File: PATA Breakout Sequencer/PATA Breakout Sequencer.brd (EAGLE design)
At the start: 100 x 70 mm, 57 parts, among them IC1 74HC165N, IC2 74HC165N, IC3 74HC165N, IC4 74HC165N, IC5 74HC165N

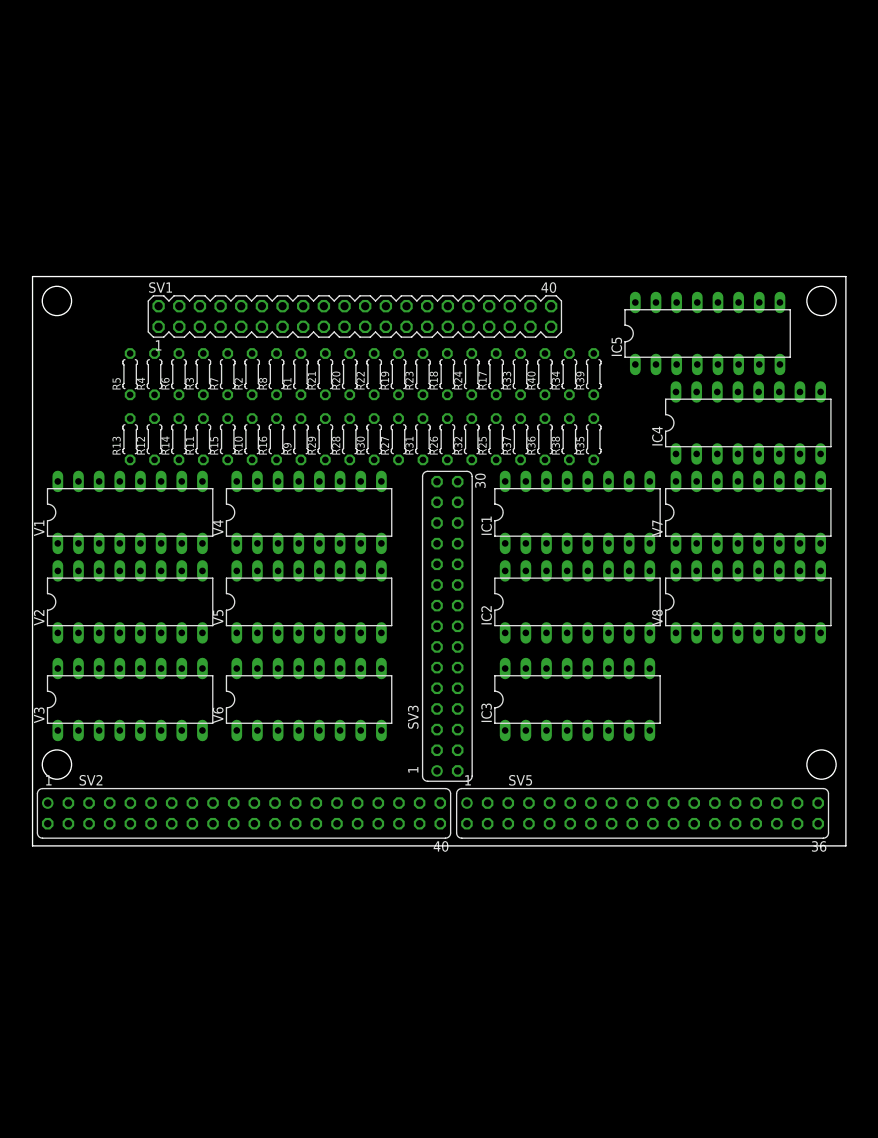
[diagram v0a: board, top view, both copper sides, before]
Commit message: split board into 2
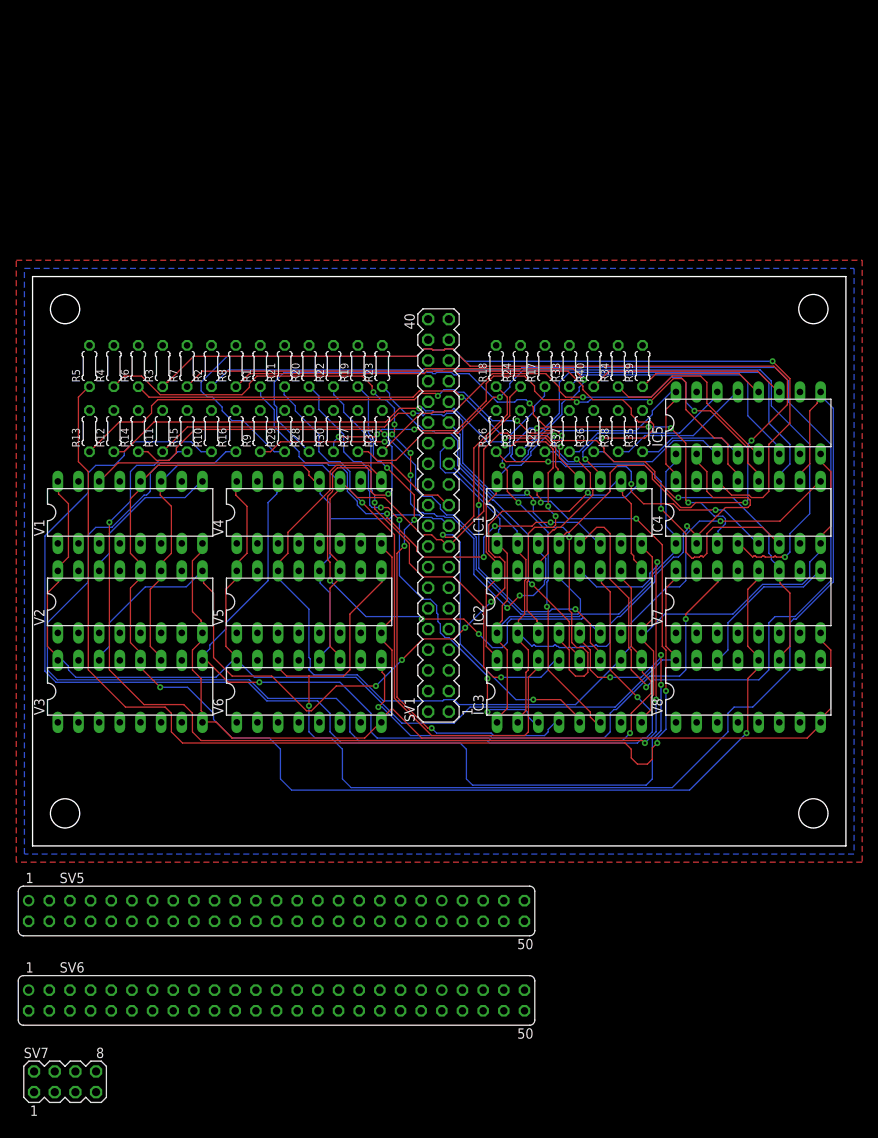
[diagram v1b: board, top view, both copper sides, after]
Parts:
- removed SV2: (no value), con-lsta:FE20-2
- removed SV3: (no value), con-lsta:FE15-2
- added SV6: (no value), con-lsta:FE25-2
- added SV7: (no value), con-lstb:MA04-2
- SV5: device con-lsta:FE18-2 -> con-lsta:FE25-2
- moved SV5 46.6 mm to (30.0, -8.00)
- moved SV1 26.5 mm to (49.9, 40.6), turned to 90 degrees
- moved IC5 12.1 mm to (88.0, 52.0)
- moved IC4 11.0 mm to (88.0, 41.0)
- moved V7 11.0 mm to (88.0, 30.0)
- moved V8 11.0 mm to (88.0, 19.0)
- moved R17 6.08 mm to (63.0, 59.0)
- moved R18 6.08 mm to (57.0, 59.0)
- moved R24 6.08 mm to (60.0, 59.0)
- moved R25 6.08 mm to (63.0, 51.0)
- moved R26 6.08 mm to (57.0, 51.0)
- moved R32 6.08 mm to (60.0, 51.0)
- moved R33 6.08 mm to (66.0, 59.0)
- moved R34 6.08 mm to (72.0, 59.0)
- moved R35 6.08 mm to (75.0, 51.0)
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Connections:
- removed net N$10: SV3.16
- removed net N$11: SV3.14
- removed net N$12: SV3.12
- removed net N$13: SV3.10
- removed net N$14: SV3.8
- removed net N$15: SV3.6
- removed net N$16: SV3.4
- removed net N$17: SV3.2
- removed net N$21: SV3.29
- removed net N$22: SV3.27
- removed net N$23: SV3.25
- removed net N$24: SV3.23
- removed net N$25: SV3.21
- removed net N$26: SV3.19
- removed net N$27: SV3.17
- removed net N$4: SV3.28
- removed net N$5: SV3.26
- removed net N$6: SV3.24
- removed net N$7: SV3.22
- removed net N$8: SV3.20
- removed net N$9: SV3.18
- net A0: now also SV6.1; no longer SV3.1, SV3.30
- net A1: now also SV6.17
- net A10: now also SV5.34
- net A11: now also SV5.50
- net A2: now also SV6.2
- net A3: now also SV5.1, SV6.18
- net A4: now also SV5.2
- net A5: now also SV5.17
- net A6: now also SV5.18
- net A7: now also SV6.33
- net A8: now also SV6.34
- net A9: now also SV5.33
- net B0: now also SV6.3; no longer SV3.3
- net B1: now also SV6.19
- net B10: now also SV5.36
- net B11: now also SV5.49
- net B2: now also SV6.4
- net B3: now also SV5.3, SV6.20
- net B4: now also SV5.4
- net B5: now also SV5.19
- net B6: now also SV5.20
- net B7: now also SV6.35
- net B8: now also SV6.36
- net B9: now also SV5.35
- net C0: now also SV6.5; no longer SV3.5
- net C1: now also SV6.21
- net C10: now also SV5.38
- net C11: now also SV6.50
- net C2: now also SV6.6
- net C3: now also SV5.5, SV6.22
- net C4: now also SV5.6
- net C5: now also SV5.21
- net C6: now also SV5.22
- net C7: now also SV6.37
- net C8: now also SV6.38
- net C9: now also SV5.37
- net D0: now also SV6.7; no longer SV3.7
- net D1: now also SV6.23
- net D10: now also SV5.40
- net D11: now also SV6.49
- net D2: now also SV6.8
- net D3: now also SV5.7, SV6.24
- net D4: now also SV5.8
- net D5: now also SV5.23
- net D6: now also SV5.24
- net D7: now also SV6.39
- net D8: now also SV6.40
- net D9: now also SV5.39
- net E0: now also SV6.9; no longer SV3.9
- net E1: now also SV6.25
- net E10: now also SV5.42
- net E11: now also SV7.8
- net E2: now also SV6.10
- net E3: now also SV5.9, SV6.26
- net E4: now also SV5.10
- net E5: now also SV5.25
- net E6: now also SV5.26
- net E7: now also SV6.41
- net E8: now also SV6.42
- net E9: now also SV5.41
- net F0: now also SV6.11; no longer SV3.11
- net F1: now also SV6.27
- net F10: now also SV5.44
- net F11: now also SV7.7
- net F2: now also SV6.12
- net F3: now also SV5.11, SV6.28
- net F4: now also SV5.12
- net F5: now also SV5.27
- net F6: now also SV5.28
- net F7: now also SV6.43
- net F8: now also SV6.44
- net F9: now also SV5.43
- net G0: now also SV6.13; no longer SV3.13
- net G1: now also SV6.29
- net G10: now also SV5.46
- net G11: now also SV7.6
- net G2: now also SV6.14
- net G3: now also SV5.13, SV6.30
- net G4: now also SV5.14
- net G5: now also SV5.29
- net G6: now also SV5.30
- net G7: now also SV6.45
- net G8: now also SV6.46
- net G9: now also SV5.45
- net H0: now also SV6.15; no longer SV3.15
- net H1: now also SV6.31
- net H10: now also SV5.48
- net H11: now also SV7.5
- net H2: now also SV6.16
- net H3: now also SV5.15, SV6.32
- net H4: now also SV5.16
- net H5: now also SV5.31
- net H6: now also SV5.32
- net H7: now also SV6.47
- net H8: now also SV6.48
- net H9: now also SV5.47
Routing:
- net LATCH_OUT: track 0.00 -> 196.4 mm, vias 0 -> 2
- net SHIFT_OUT: track 0.00 -> 161.6 mm, vias 0 -> 1
- net D0: track 0.00 -> 159.6 mm, vias 0 -> 4
- net G1: track 0.00 -> 159.5 mm, vias 0 -> 3
- net G0: track 0.00 -> 156.7 mm, vias 0 -> 1
- net OUT4: track 0.00 -> 151.9 mm, vias 0 -> 1
- net +UB: track 0.00 -> 145.1 mm
- net A1: track 0.00 -> 144.9 mm, vias 0 -> 1
- net B1: track 0.00 -> 139.5 mm, vias 0 -> 4
- net -UB: track 0.00 -> 139.2 mm
- net F0: track 0.00 -> 129.0 mm, vias 0 -> 2
- net OUT3: track 0.00 -> 117.9 mm, vias 0 -> 1
- net OUT1: track 0.00 -> 115.3 mm, vias 0 -> 5
- net D3: track 0.00 -> 112.9 mm, vias 0 -> 1
- net OUT2: track 0.00 -> 106.8 mm, vias 0 -> 2
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- added copper zone on layer 1, net +5V
- added copper zone on layer 16, net DGND

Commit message: Finished top board - ran DRC
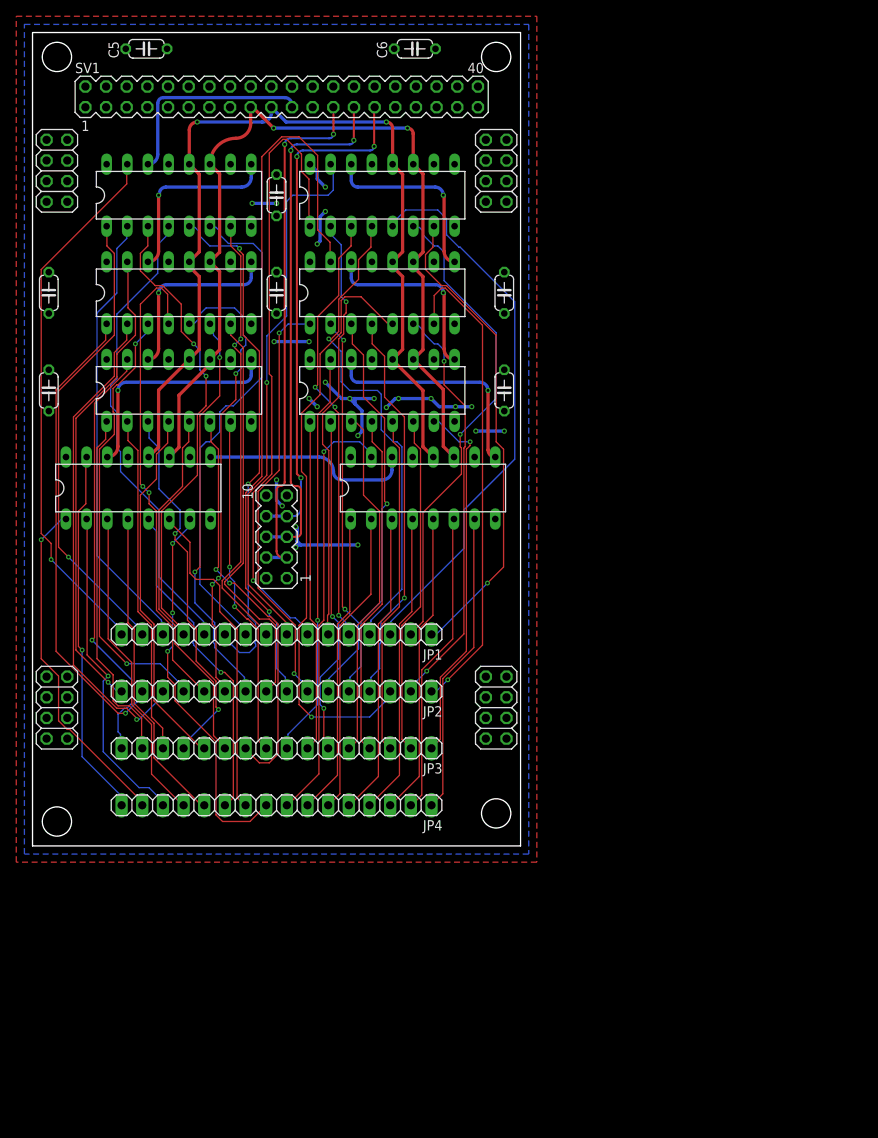
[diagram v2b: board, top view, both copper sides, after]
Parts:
- removed IC1, IC2, IC3, IC4, IC5: 74HC165N, 74xx-eu:DIL16
- removed R1, R10, R11, R12, R13, R14, R15, R16, R17, R18, R19, R2, R20, R21, R22, R23, R24, R25, R26, R27, R28, R29, R3, R30, R31, R32, R33, R34, R35, R36, R37, R38, R39, R4, R40, R5, R6, R7, R8, R9: (no value), rcl:0204/5
- removed SV5, SV6: (no value), con-lsta:FE25-2
- removed SV7: (no value), con-lstb:MA04-2
- added C1, C2, C3, C4, C5, C6, C7, C8: 4.7uF, rcl:C050-024X044
- added JP1, JP2, JP3, JP4: (no value), pinhead:1X16
- added JP6, JP7, JP8, JP9: (no value), pinhead:2X04
- added SV3: (no value), con-lstb:MA05-2
- moved V8 75.8 mm to (43.0, 80.0)
- moved V7 58.9 mm to (43.0, 68.0)
- moved SV1 55.0 mm to (30.6, 92.1), turned to 0 degrees
- moved V1 39.5 mm to (18.0, 80.0)
- moved V2 38.5 mm to (18.0, 68.0)
- moved V6 38.1 mm to (43.0, 56.0)
- moved V3 37.5 mm to (18.0, 56.0)
- moved V4 21.2 mm to (13.0, 44.0)
- moved V5 19.8 mm to (48.0, 44.0)
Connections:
- removed net +5V: R1.2, R10.2, R11.2, R12.2, R13.2, R14.2, R15.2, R16.2, R17.2, R18.2, R19.2, R2.2, R20.2, R21.2, R22.2, R23.2, R24.2, R25.2, R26.2, R27.2, R28.2, R29.2, R3.2, R30.2, R31.2, R32.2, R33.2, R34.2, R35.2, R36.2, R37.2, R38.2, R39.2, R4.2, R40.2, R5.2, R6.2, R7.2, R8.2, R9.2, SV1.2, SV1.4, SV1.6
- removed net A0: IC1.11, R8.1, SV6.1
- removed net A1: IC2.11, R16.1, SV6.17
- removed net A2: IC3.11, R24.1, SV6.2
- removed net A3: IC4.11, R32.1, SV5.1, SV6.18
- removed net A4: IC5.11, R40.1, SV5.2
- removed net B0: IC1.12, R7.1, SV6.3
- removed net B1: IC2.12, R15.1, SV6.19
- removed net B2: IC3.12, R23.1, SV6.4
- removed net B3: IC4.12, R31.1, SV5.3, SV6.20
- removed net B4: IC5.12, R39.1, SV5.4
- removed net C0: IC1.13, R6.1, SV6.5
- removed net C1: IC2.13, R14.1, SV6.21
- removed net C2: IC3.13, R22.1, SV6.6
- removed net C3: IC4.13, R30.1, SV5.5, SV6.22
- removed net C4: IC5.13, R38.1, SV5.6
- removed net D0: IC1.14, R5.1, SV6.7
- removed net D1: IC2.14, R13.1, SV6.23
- removed net D2: IC3.14, R21.1, SV6.8
- removed net D3: IC4.14, R29.1, SV5.7, SV6.24
- removed net D4: IC5.14, R37.1, SV5.8
- removed net DGND: IC1.15, IC2.15, IC3.15, IC4.15, IC5.10, IC5.15, SV1.1, SV1.10, SV1.11, SV1.12, SV1.14, SV1.15, SV1.16, SV1.18, SV1.20, SV1.22, SV1.23, SV1.24, SV1.26, SV1.28, SV1.3, SV1.30, SV1.31, SV1.32, SV1.33, SV1.34, SV1.5, SV1.7, SV1.8, V1.13, V2.13, V3.13, V4.13, V5.13, V6.13, V7.13, V8.13
- removed net E0: IC1.3, R4.1, SV6.9
- removed net E1: IC2.3, R12.1, SV6.25
- removed net E2: IC3.3, R20.1, SV6.10
- removed net E3: IC4.3, R28.1, SV5.9, SV6.26
- removed net E4: IC5.3, R36.1, SV5.10
- removed net F0: IC1.4, R3.1, SV6.11
- removed net F1: IC2.4, R11.1, SV6.27
- removed net F2: IC3.4, R19.1, SV6.12
- removed net F3: IC4.4, R27.1, SV5.11, SV6.28
- removed net F4: IC5.4, R35.1, SV5.12
- removed net G0: IC1.5, R2.1, SV6.13
- removed net G1: IC2.5, R10.1, SV6.29
- removed net G2: IC3.5, R18.1, SV6.14
- removed net G3: IC4.5, R26.1, SV5.13, SV6.30
- removed net G4: IC5.5, R34.1, SV5.14
- removed net GND: IC1.8, IC2.8, IC3.8, IC4.8, IC5.8
- removed net H0: IC1.6, R1.1, SV6.15
- removed net H1: IC2.6, R9.1, SV6.31
- removed net H2: IC3.6, R17.1, SV6.16
- removed net H3: IC4.6, R25.1, SV5.15, SV6.32
- removed net H4: IC5.6, R33.1, SV5.16
- removed net VCC: IC1.16, IC2.16, IC3.16, IC4.16, IC5.16
- net +UB: now also C1.1, C2.1, C3.1, C4.1, C5.1, C6.1, C7.1, C8.1, JP6.1, JP6.3, JP6.5, JP6.7, JP7.1, JP7.3, JP7.5, JP7.7, JP8.1, JP8.3, JP8.5, JP8.7, JP9.1, JP9.3, JP9.5, JP9.7, SV1.2, SV1.4, SV1.6, SV3.2, SV3.9
- net -UB: now also C1.2, C2.2, C3.2, C4.2, C5.2, C6.2, C7.2, C8.2, JP6.2, JP6.4, JP6.6, JP6.8, JP7.2, JP7.4, JP7.6, JP7.8, JP8.2, JP8.4, JP8.6, JP8.8, JP9.2, JP9.4, JP9.6, JP9.8, SV1.1, SV1.10, SV1.11, SV1.12, SV1.14, SV1.15, SV1.16, SV1.18, SV1.20, SV1.22, SV1.23, SV1.24, SV1.26, SV1.28, SV1.3, SV1.30, SV1.31, SV1.32, SV1.33, SV1.34, SV1.5, SV1.7, SV1.8, SV3.1, SV3.10, V1.13, V2.13, V3.13, V4.13, V5.13, V6.13, V7.13, V8.13
- net A10: now also JP3.8; no longer SV5.34
- net A11: now also JP2.8; no longer SV5.50
- net A12: now also JP1.8
- net A5: now also JP1.16; no longer SV5.17
- net A6: now also JP2.16; no longer SV5.18
- net A7: now also JP3.16; no longer SV6.33
- net A8: now also JP4.16; no longer SV6.34
- net A9: now also JP4.8; no longer SV5.33
- net B10: now also JP3.7; no longer SV5.36
- net B11: now also JP2.7; no longer SV5.49
- net B12: now also JP1.7
- net B5: now also JP1.15; no longer SV5.19
- net B6: now also JP2.15; no longer SV5.20
- net B7: now also JP3.15; no longer SV6.35
- net B8: now also JP4.15; no longer SV6.36
- net B9: now also JP4.7; no longer SV5.35
- net C10: now also JP3.6; no longer SV5.38
- net C11: now also JP2.6; no longer SV6.50
- net C12: now also JP1.6
- net C5: now also JP1.14; no longer SV5.21
- net C6: now also JP2.14; no longer SV5.22
- net C7: now also JP3.14; no longer SV6.37
- net C8: now also JP4.14; no longer SV6.38
- net C9: now also JP4.6; no longer SV5.37
- net D10: now also JP3.5; no longer SV5.40
- net D11: now also JP2.5; no longer SV6.49
- net D12: now also JP1.5
- net D5: now also JP1.13; no longer SV5.23
- net D6: now also JP2.13; no longer SV5.24
- net D7: now also JP3.13; no longer SV6.39
- net D8: now also JP4.13; no longer SV6.40
- net D9: now also JP4.5; no longer SV5.39
- net E10: now also JP3.4; no longer SV5.42
- net E11: now also JP2.4; no longer SV7.8
- net E12: now also JP1.4
- net E5: now also JP1.12; no longer SV5.25
- net E6: now also JP2.12; no longer SV5.26
- net E7: now also JP3.12; no longer SV6.41
- net E8: now also JP4.12; no longer SV6.42
- net E9: now also JP4.4; no longer SV5.41
- net F10: now also JP3.3; no longer SV5.44
- net F11: now also JP2.3; no longer SV7.7
- net F12: now also JP1.3
- net F5: now also JP1.11; no longer SV5.27
- net F6: now also JP2.11; no longer SV5.28
- net F7: now also JP3.11; no longer SV6.43
- net F8: now also JP4.11; no longer SV6.44
- net F9: now also JP4.3; no longer SV5.43
- net G10: now also JP3.2; no longer SV5.46
- net G11: now also JP2.2; no longer SV7.6
- net G12: now also JP1.2
- net G5: now also JP1.10; no longer SV5.29
- net G6: now also JP2.10; no longer SV5.30
- net G7: now also JP3.10; no longer SV6.45
- net G8: now also JP4.10; no longer SV6.46
- net G9: now also JP4.2; no longer SV5.45
- net H10: now also JP3.1; no longer SV5.48
- net H11: now also JP2.1; no longer SV7.5
- net H12: now also JP1.1
- net H5: now also JP1.9; no longer SV5.31
- net H6: now also JP2.9; no longer SV5.32
- net H7: now also JP3.9; no longer SV6.47
- net H8: now also JP4.9; no longer SV6.48
- net H9: now also JP4.1; no longer SV5.47
- net LATCH_IN: now also SV3.5, SV3.6; no longer IC1.1, IC2.1, IC3.1, IC4.1, IC5.1
- net OUT1: no longer IC1.10, IC2.9
- net OUT2: no longer IC2.10, IC3.9
- net OUT3: no longer IC3.10, IC4.9
- net OUT4: no longer IC4.10, IC5.9
- net SERIAL_IN: now also SV3.7, SV3.8; no longer IC1.9
- net SHIFT_IN: now also SV3.3, SV3.4; no longer IC1.2, IC2.2, IC3.2, IC4.2, IC5.2
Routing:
- net D0: track 159.6 -> 0.00 mm, vias 4 -> 0
- net G1: track 159.5 -> 0.00 mm, vias 3 -> 0
- net G0: track 156.7 -> 0.00 mm, vias 1 -> 0
- net A1: track 144.9 -> 0.00 mm, vias 1 -> 0
- net B1: track 139.5 -> 0.00 mm, vias 4 -> 0
- net -UB: track 139.2 -> 0.00 mm
- net F0: track 129.0 -> 0.00 mm, vias 2 -> 0
- net OUT4: track 151.9 -> 28.1 mm
- net D3: track 112.9 -> 0.00 mm, vias 1 -> 0
- net OUT1: track 115.3 -> 22.8 mm, vias 5 -> 1
- net OUT3: track 117.9 -> 25.6 mm, vias 1 -> 0
- net A11: track 0.00 -> 91.3 mm, vias 0 -> 1
- net F1: track 89.2 -> 0.00 mm, vias 4 -> 0
- net F3: track 88.6 -> 0.00 mm, vias 2 -> 0
- net H1: track 87.1 -> 0.00 mm, vias 5 -> 0
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- added copper zone on layer 1, net +UB
- added copper zone on layer 16, net -UB
- removed copper zone on layer 1, net +5V
- removed copper zone on layer 16, net DGND
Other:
- board size 100 x 70 mm -> 60 x 100 mm

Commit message: cleanup
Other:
- board text added: "1"
- board text added: "A"
- board text added: "H"
- board text added: "Koltin Kosik-Harvey March 7 / 2019"
- board text added: "PATA Sequencer Breakout TOP"
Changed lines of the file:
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@@
 <hole x="57" y="4" drill="3.6"/>
 <hole x="57" y="97" drill="3.6"/>
+<wire x1="30" y1="30" x2="30" y2="24" width="0.1524" layer="21"/>
+<wire x1="30" y1="21" x2="30" y2="17" width="0.1524" layer="21"/>
+<wire x1="30" y1="14" x2="30" y2="10" width="0.1524" layer="21"/>
+<wire x1="30" y1="7" x2="30" y2="3" width="0.1524" layer="21"/>
+<wire x1="10" y1="3" x2="10" y2="7" width="0.1524" layer="21"/>
+<wire x1="10" y1="10" x2="10" y2="14" width="0.1524" layer="21"/>
+<wire x1="10" y1="21" x2="10" y2="17" width="0.1524" layer="21"/>
+<wire x1="51" y1="21" x2="51" y2="17" width="0.1524" layer="21"/>
+<wire x1="51" y1="14" x2="51" y2="10" width="0.1524" layer="21"/>
+<wire x1="51" y1="7" x2="51" y2="3" width="0.1524" layer="21"/>
+<wire x1="10" y1="28" x2="10" y2="24" width="0.1524" layer="21"/>
+<text x="10" y="28" size="1.778" layer="21">A</text>
+<text x="30.5" y="28" size="1.778" layer="21">A</text>
+<text x="27.7" y="28" size="1.778" layer="21">H</text>
+<text x="48" y="28" size="1.778" layer="21">H</text>
+<text x="6.45" y="79" size="1.778" layer="21">1</text>
+<text x="3" y="30" size="1.778" layer="21">PATA Sequencer
+Breakout
+TOP</text>
+<text x="36" y="32" size="1.778" layer="21">Koltin Kosik-Harvey
+March 7 / 2019</text>
 </plain>
 <attributes>
@@
 </drawing>
 <compatibility>
+<note version="6.3" minversion="6.2.2" severity="warning">
+Since Version 6.2.2 text objects can contain more than one line,
+which will not be processed correctly with this version.
+</note>
 <note version="8.2" severity="warning">
 Since Version 8.2, EAGLE supports online libraries. The ids
